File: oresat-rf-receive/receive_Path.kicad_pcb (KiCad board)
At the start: 4 copper layers, 50.7 x 68.4 mm, 32 parts, among them J1 Conn_Coaxial_142-0711-201, J2 0022232041, J3 0022232021, J5 0022232021, J6 Conn_Coaxial_142-0711-201, U1 TQP3M9037, U2 PAT1220-C-3DB, U3 SN74LVC1G32QDBVRQ1, U4 PAT1220-C-3DB, U5 TQP3M9037, U6 PD2328J5050S2HF, U7 LTC5505-1ES5

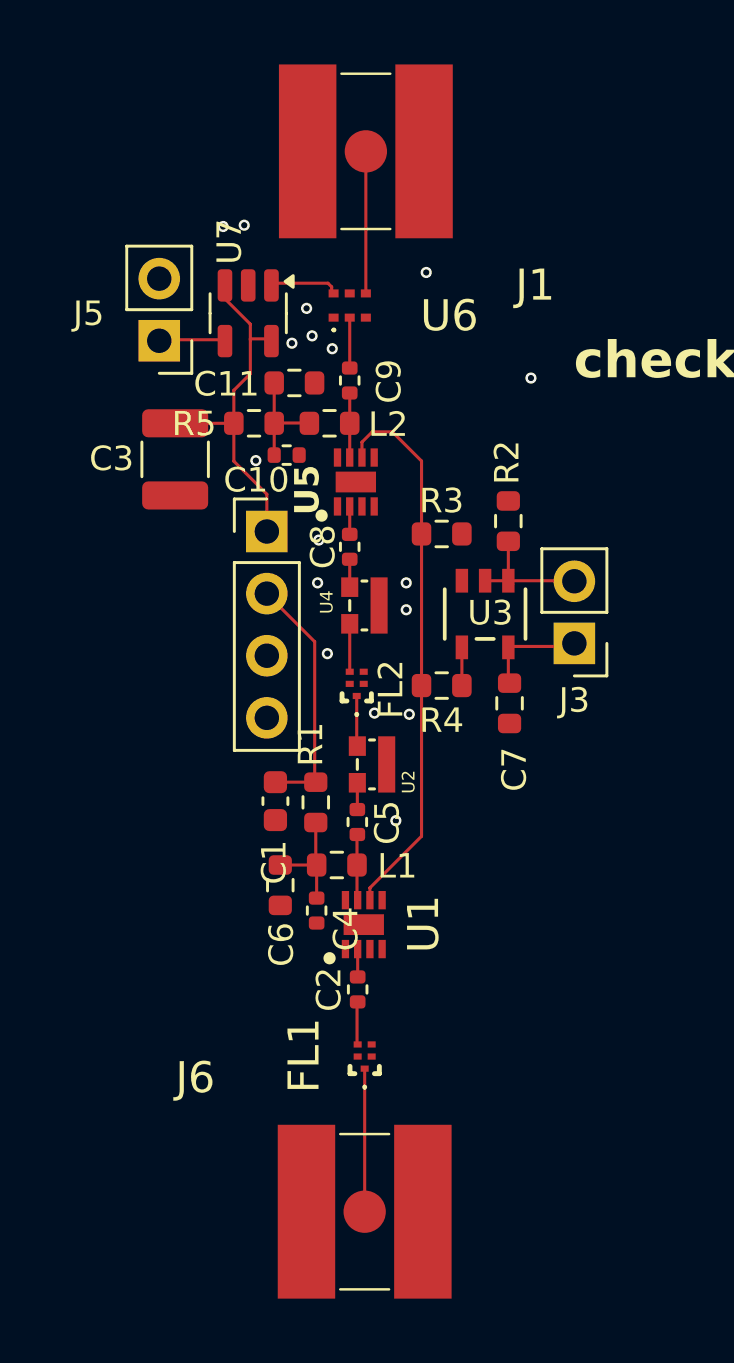
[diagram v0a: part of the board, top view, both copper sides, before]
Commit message: update traces and net class
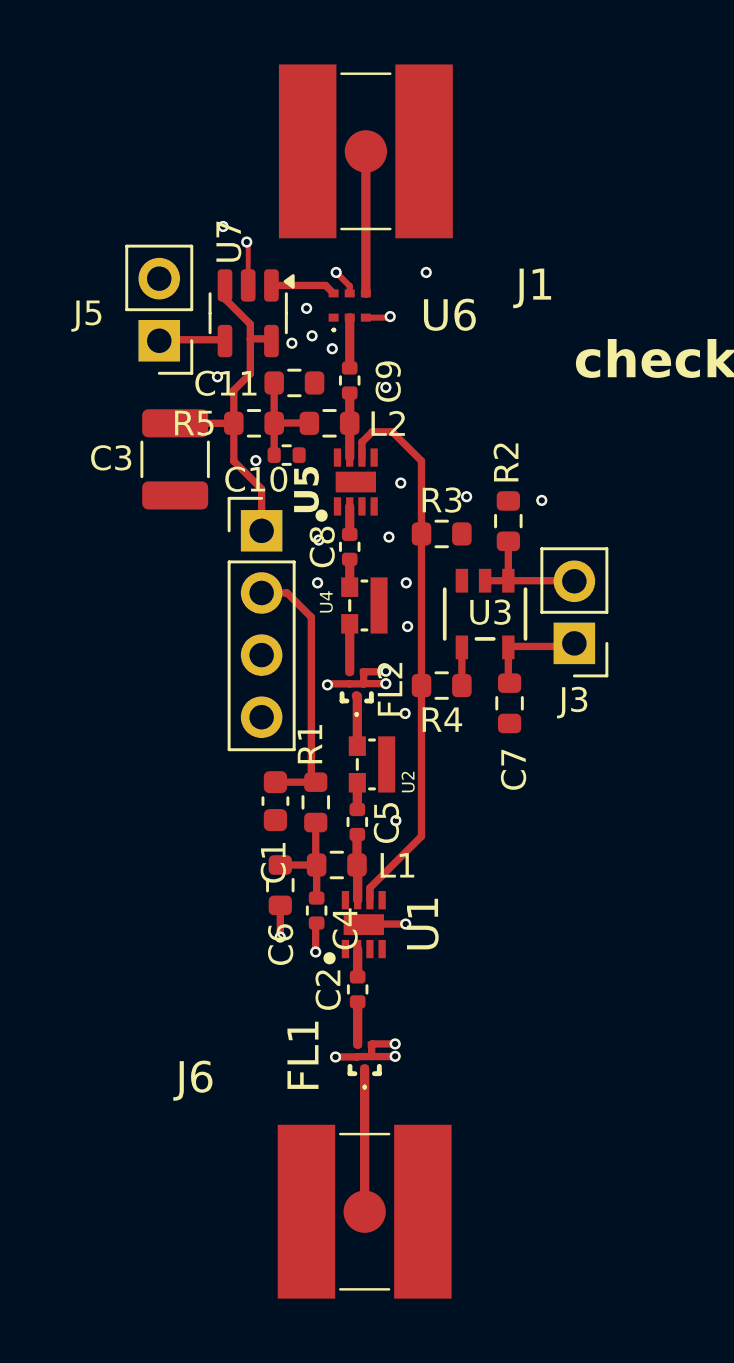
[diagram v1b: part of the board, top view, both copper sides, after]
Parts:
- moved J2 0.22 mm to (121.4, 107.8)
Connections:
- net /RF_OUT renamed /RF_OUT1
- net Net-(C5-Pad2) renamed /RF_LNA1_OUT2
- net Net-(FL1-OUTPUT) renamed /RF_BPF_OUT1
- net Net-(FL2-INPUT) renamed /RF_ATTEN1_OUT1
- net Net-(FL2-OUTPUT) renamed /RF_BPF2_OUT
- net Net-(U1-RF_IN) renamed /RF_BPF_OUT2
- net Net-(U1-RF_OUT) renamed /RF_LNA1_OUT1
- net Net-(U6-OUTPUT2) renamed /PWR_DET_IN
- C8 pad 1: Net-(C8-Pad1) -> /RF_ATTEN2_OUT1
- C8 pad 2: Net-(U5-RF_IN) -> /RF_ATTEN2_OUT2
- C9 pad 1: Net-(U5-RF_OUT) -> /RF_ATTEN2_OUT1
- C9 pad 2: Net-(U6-INPUT) -> /RF_ATTEN2_OUT2
- L2 pad 2: Net-(U5-RF_OUT) -> /RF_ATTEN2_OUT1
- U4 pad 2: Net-(C8-Pad1) -> /RF_ATTEN2_OUT1
- U5 pad 2: Net-(U5-RF_IN) -> /RF_ATTEN2_OUT2
- U5 pad 7: Net-(U5-RF_OUT) -> /RF_ATTEN2_OUT1
- U6 pad 2: Net-(U6-INPUT) -> /RF_ATTEN2_OUT2
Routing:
- net GND: track 0.02 -> 15.9 mm, vias 17 -> 31
- net /RF_ATTEN2_OUT1: track 0.00 -> 3.69 mm
- net /RF_ATTEN2_OUT2: track 0.00 -> 3.20 mm
- net Net-(U5-RF_OUT): track 2.64 -> 0.00 mm
- net Net-(U6-INPUT): track 2.06 -> 0.00 mm
- net Net-(U5-RF_IN): track 1.14 -> 0.00 mm
- net Net-(C8-Pad1): track 1.14 -> 0.00 mm
- net 5VA: track 42.9 -> 43.7 mm

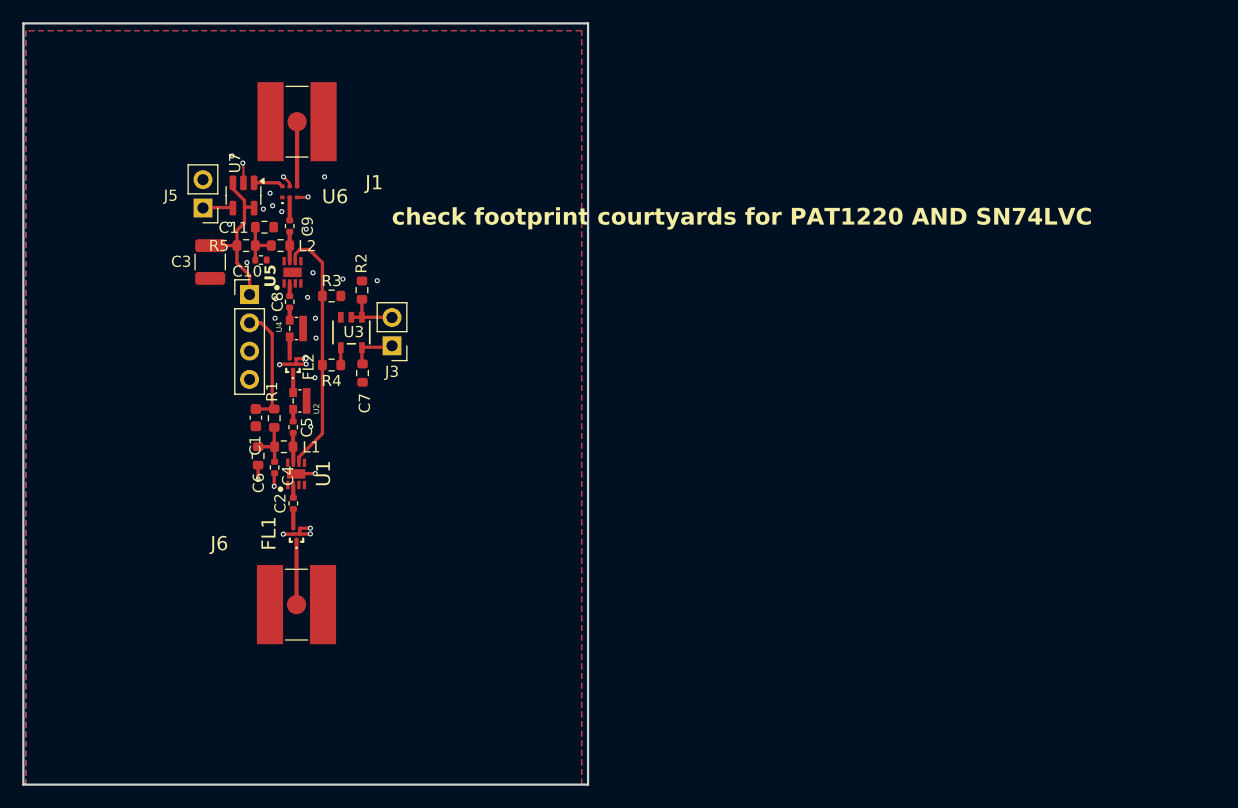
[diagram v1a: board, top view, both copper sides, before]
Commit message: Updated board layout, traces widths, and silkscreen
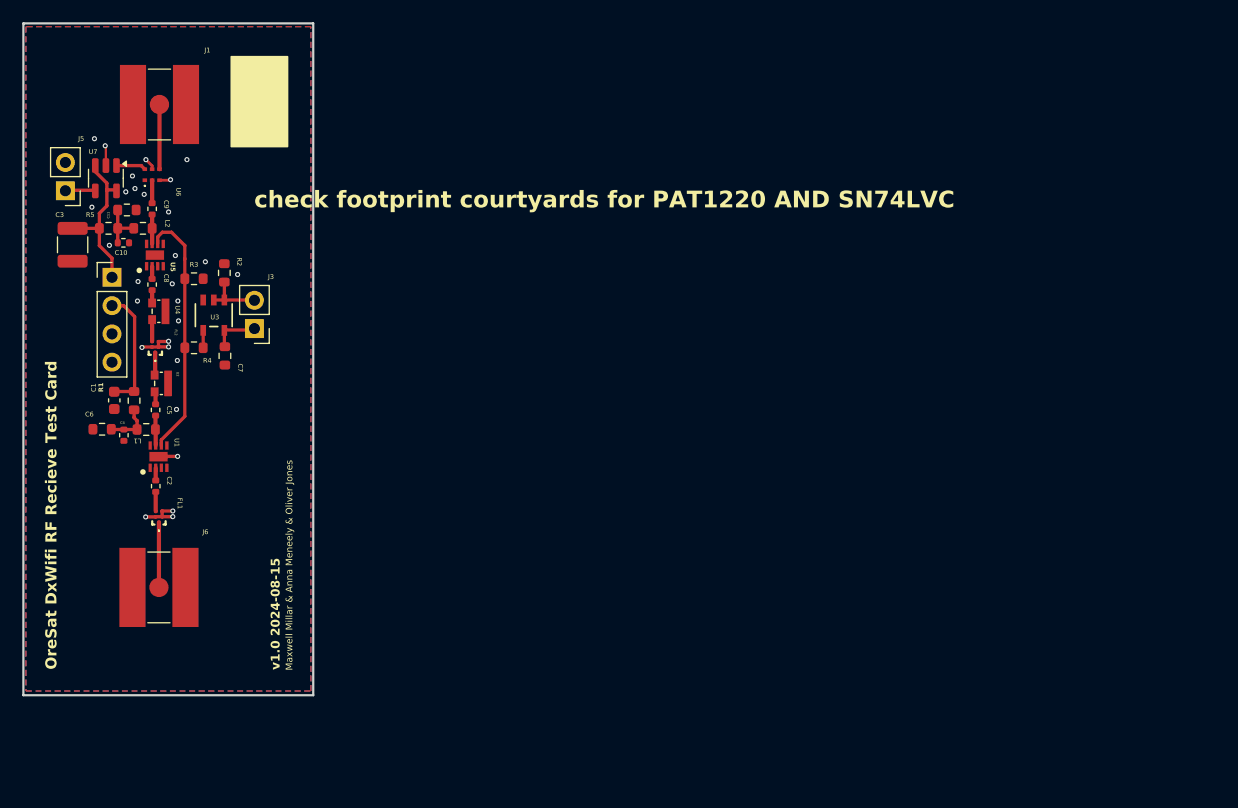
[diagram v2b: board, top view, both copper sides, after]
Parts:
- moved C6 14.2 mm to (108.1, 119.9), turned to 180 degrees
- moved C4 13.8 mm to (110.1, 120.5)
- moved C1 12.8 mm to (109.2, 117.4)
- moved R1 12.7 mm to (111.0, 117.4)
- moved U2 12.5 mm to (113.5, 115.8)
- moved J3 12.5 mm to (121.8, 110.9)
- moved C5 12.5 mm to (112.9, 118.2)
- moved C7 12.5 mm to (119.2, 113.4)
- moved C9 12.5 mm to (112.6, 100.2)
- moved FL2 12.5 mm to (112.9, 112.6)
- moved J5 12.5 mm to (104.8, 98.5)
- moved J6 12.5 mm to (113.2, 134.1)
- moved L1 12.5 mm to (112.1, 120.0)
- moved L2 12.5 mm to (111.8, 101.9)
- moved R2 12.5 mm to (119.1, 105.9)
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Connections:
- C9 pad 1: /RF_ATTEN2_OUT1 -> /RF_LNA2_OUT1
- C9 pad 2: /RF_ATTEN2_OUT2 -> /RF_LNA2_OUT2
- L2 pad 2: /RF_ATTEN2_OUT1 -> /RF_LNA2_OUT1
- U5 pad 7: /RF_ATTEN2_OUT1 -> /RF_LNA2_OUT1
- U6 pad 2: /RF_ATTEN2_OUT2 -> /RF_LNA2_OUT2
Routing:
- net 5VA: track 43.7 -> 29.6 mm
- net /RF_ATTEN2_OUT1: track 3.69 -> 1.09 mm
- net /RF_LNA2_OUT1: track 0.00 -> 2.59 mm
- net GND: track 15.9 -> 13.4 mm, vias 31 -> 29
- net /RF_LNA2_OUT2: track 0.00 -> 2.06 mm
- net /RF_ATTEN2_OUT2: track 3.20 -> 1.14 mm
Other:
- board size 50.7 x 68.4 mm -> 26 x 60.3 mm
- board text added: "${REVISION} ${ISSUE_DATE}"
- board text added: "Maxwell Millar & Anna Meneely & Oliver Jones"
- board text added: "OreSat DxWifi RF Recieve Test Card"
- board text added: "v1.0 2024-08-15"

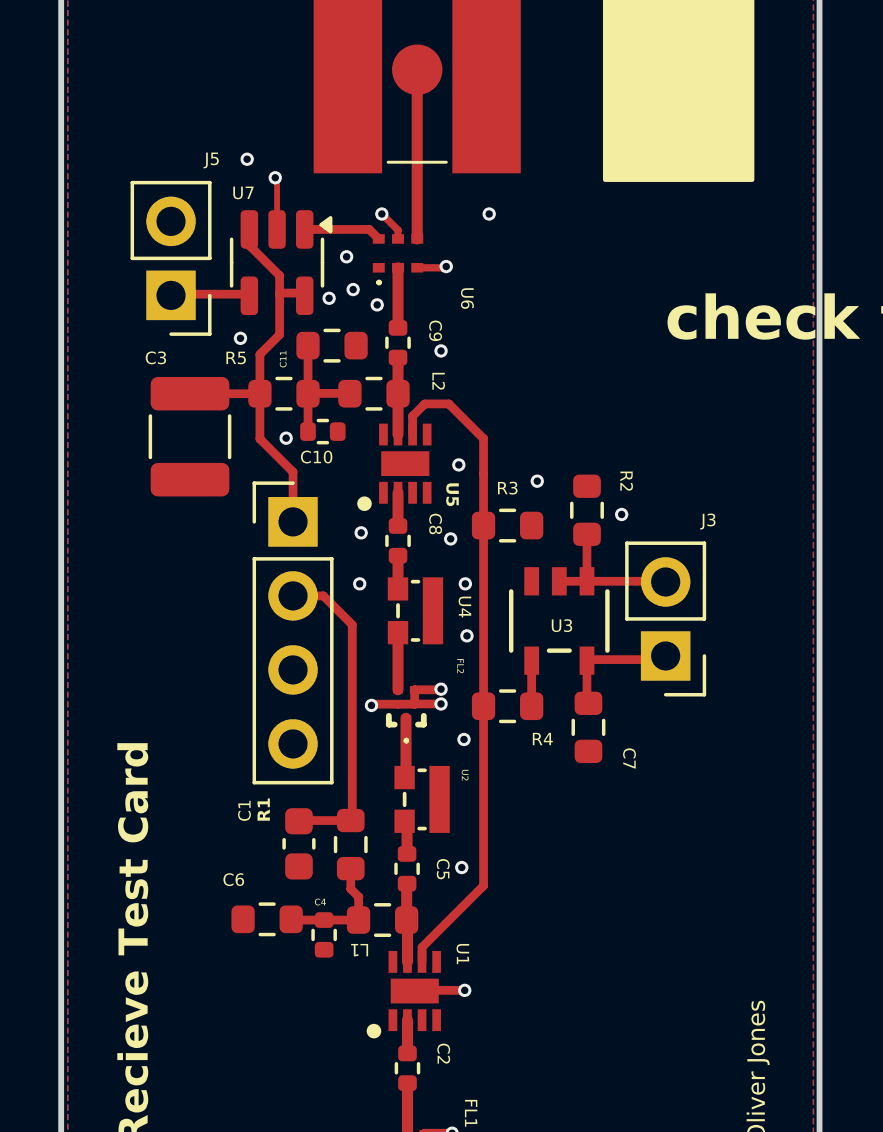
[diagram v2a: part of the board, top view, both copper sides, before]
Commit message: modified 5V power connections on PCB
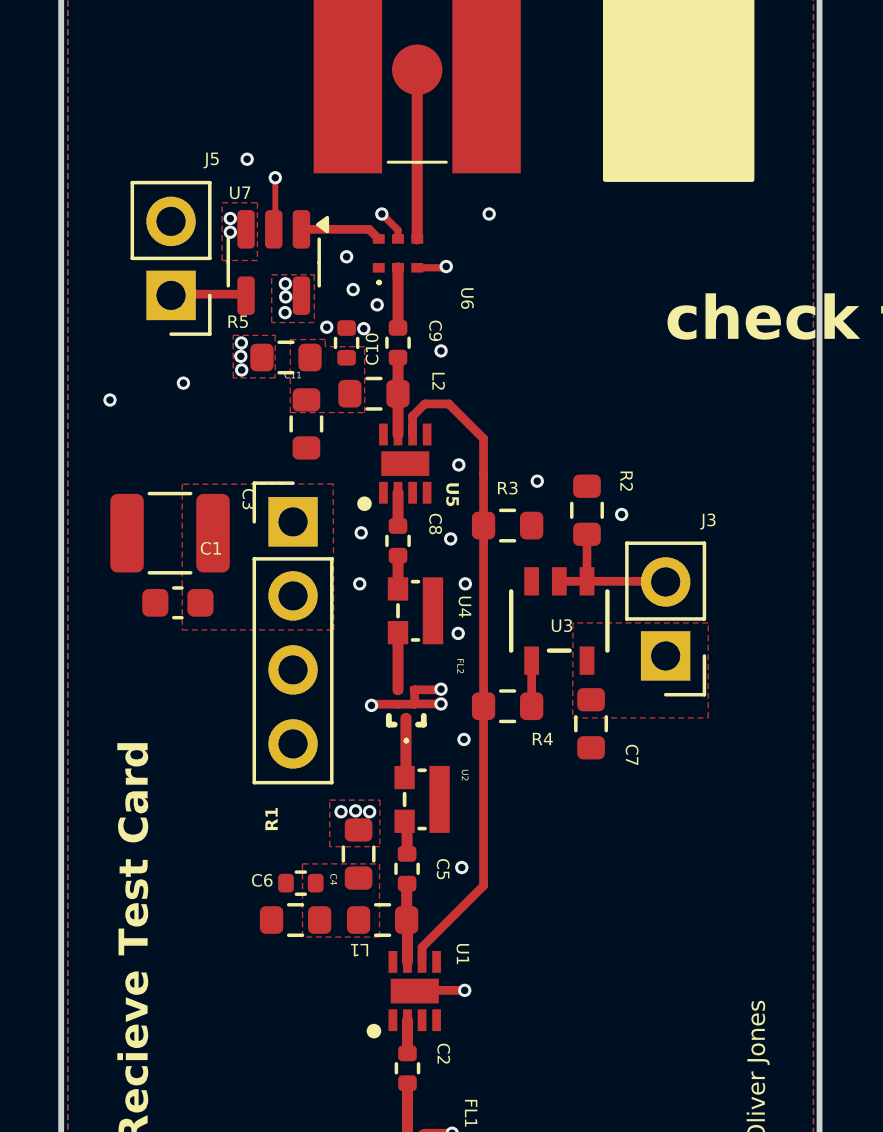
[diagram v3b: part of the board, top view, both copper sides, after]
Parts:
- moved C1 9.26 mm to (105.1, 109.1), turned to 180 degrees
- moved C3 3.38 mm to (104.8, 106.7), turned to 180 degrees
- moved C10 3.15 mm to (110.9, 100.2), turned to 90 degrees
- moved C11 2.83 mm to (109.5, 102.9), turned to -90 degrees
- moved C4 1.95 mm to (109.3, 118.7), turned to 180 degrees
- moved R5 1.25 mm to (108.8, 100.7)
- moved C6 0.98 mm to (109.1, 120.0)
- moved R1 0.42 mm to (111.3, 117.7)
- moved C7 0.15 mm to (119.3, 113.2)
- moved U7 0.11 mm to (108.4, 97.4)
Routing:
- net 5VA: track 29.6 -> 0.25 mm, vias 0 -> 11
- net Net-(C10-Pad1): track 4.25 -> 0.00 mm
- net Net-(C4-Pad1): track 4.24 -> 0.00 mm
- net GND: vias 29 -> 30
- added copper zone on F.Cu, net 5VA
- added copper zone on F.Cu, net Net-(C10-Pad1)
- added copper zone on F.Cu, net Net-(C4-Pad1)
